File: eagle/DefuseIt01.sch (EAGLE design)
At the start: 32 parts, among them IC1 74HCT138N, IC2 74HCT138N, IC3 74HCT245N, J1 22-27-2061-06, J10 22-27-2061-06, J11 22-27-2061-06, J12 22-27-2061-06, J13 22-27-2061-06, J14 22-27-2061-06, J15 22-27-2061-06, J16 22-27-2061-06, J17 22-27-2021-02, J18 22-27-2031-03, J19 22-27-2031-03, J2 22-27-2061-06, J20 22-27-2021-02, J3 22-27-2061-06, J4 22-27-2061-06, J5 22-27-2061-06, J6 22-27-2061-06, J7 22-27-2061-06, J8 22-27-2061-06, J9 22-27-2061-06

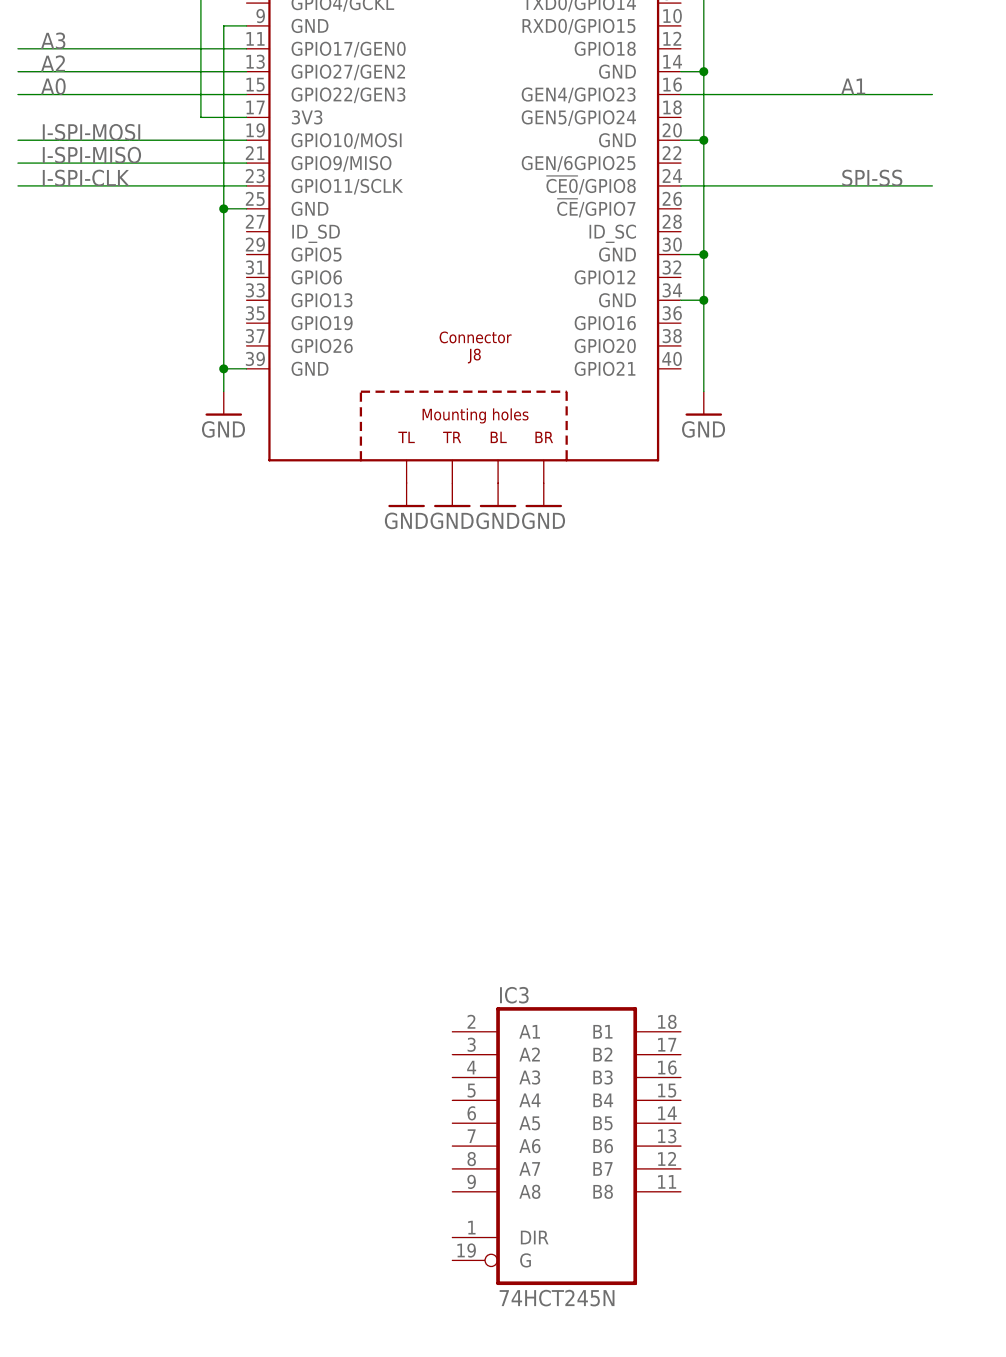
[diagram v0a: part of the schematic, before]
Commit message: Finished first layout w/o audio
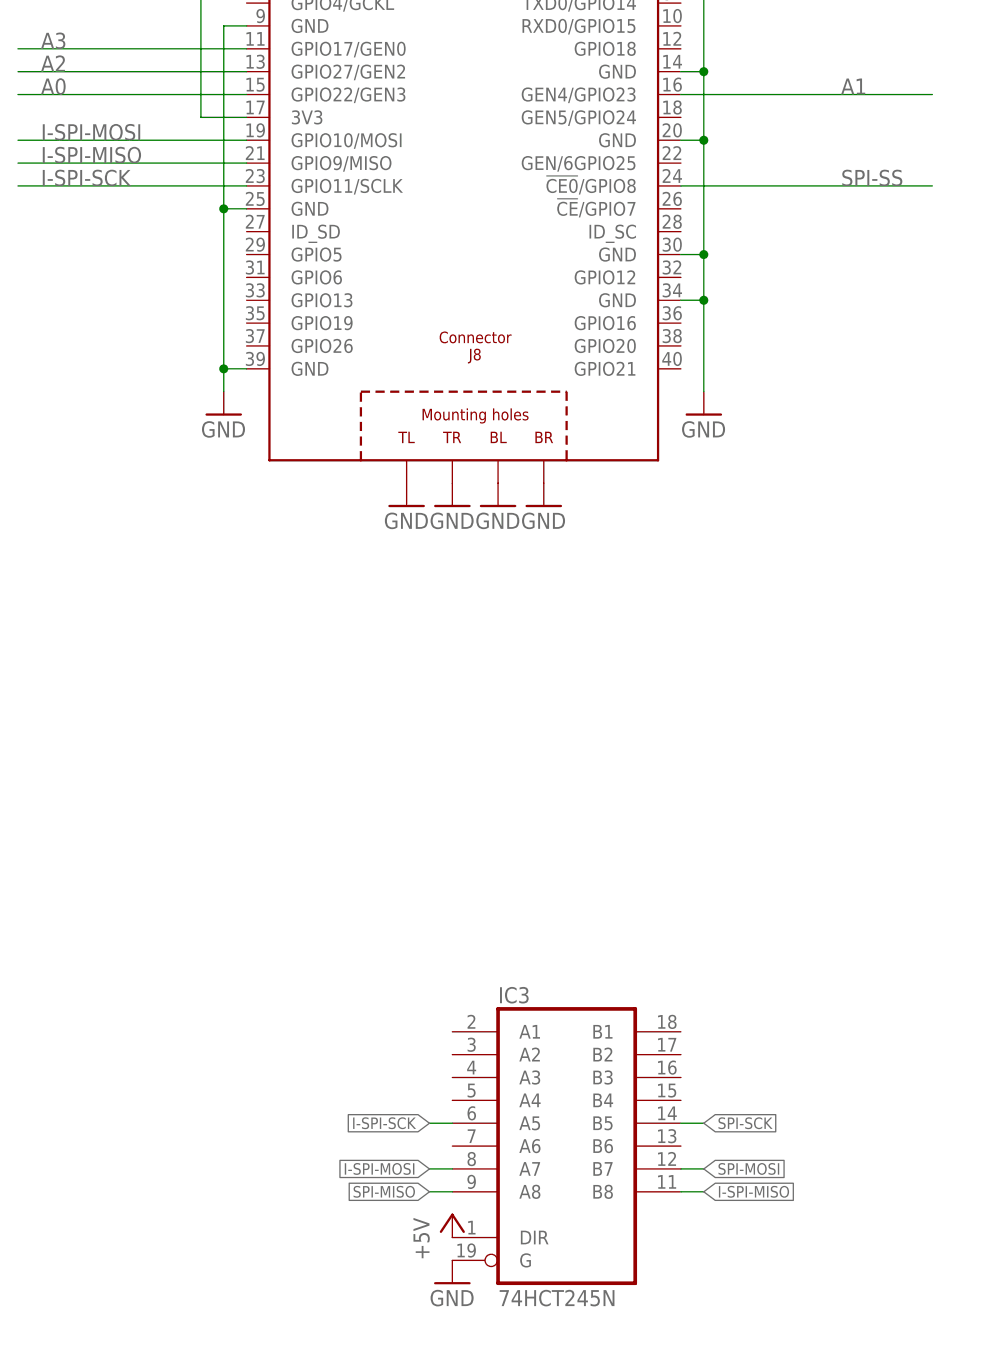
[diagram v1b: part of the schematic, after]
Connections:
- removed net I-SPI-CLK: PCB1.GPIO11/SCLK
- new net I-SPI-SCK: IC3A.A5, PCB1.GPIO11/SCLK
- new net SPI-SCK: IC3A.B5
- net +5V: now also IC3A.DIR
- net GND: now also IC3A.G
- net I-SPI-MISO: now also IC3A.B8
- net I-SPI-MOSI: now also IC3A.A7
- net SPI-MISO: now also IC3A.A8
- net SPI-MOSI: now also IC3A.B7
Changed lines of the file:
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@@
 <part name="J17" library="con-molex" deviceset="22-?-02" device="27-2021"/>
 <part name="J20" library="con-molex" deviceset="22-?-02" device="27-2021"/>
+<part name="P+7" library="supply1" deviceset="+5V" device=""/>
+<part name="GND11" library="supply1" deviceset="GND" device=""/>
 </parts>
 <sheets>
@@
 <instance part="J15" gate="-6" x="200.66" y="17.78" rot="R270"/>
 <instance part="J16" gate="-6" x="200.66" y="7.62" rot="R270"/>
+<instance part="P+7" gate="1" x="55.88" y="-7.62"/>
+<instance part="GND11" gate="1" x="55.88" y="-15.24"/>
 </instances>
 <busses>
@@
 <junction x="226.06" y="149.86"/>
 </segment>
+<segment>
+<pinref part="IC3" gate="A" pin="G"/>
+<pinref part="GND11" gate="1" pin="GND"/>
+</segment>
 </net>
 <net name="+5V" class="0">
@@
 <wire x1="220.98" y1="172.72" x2="220.98" y2="160.02" width="0.1524" layer="91"/>
 <junction x="220.98" y="160.02"/>
+</segment>
+<segment>
+<pinref part="IC3" gate="A" pin="DIR"/>
+<pinref part="P+7" gate="1" pin="+5V"/>
 </segment>
 </net>
@@
 <label x="172.72" y="167.64" size="1.778" layer="95"/>
 </segment>
+<segment>
+<pinref part="IC3" gate="A" pin="B7"/>
+<wire x1="81.28" y1="-2.54" x2="83.82" y2="-2.54" width="0.1524" layer="91"/>
+<label x="83.82" y="-2.54" size="1.27" layer="95" xref="yes"/>
+</segment>
 </net>
 <net name="SPI-MISO" class="0">
@@
 <label x="172.72" y="165.1" size="1.778" layer="95"/>
 </segment>
+<segment>
+<pinref part="IC3" gate="A" pin="A8"/>
+<wire x1="55.88" y1="-5.08" x2="53.34" y2="-5.08" width="0.1524" layer="91"/>
+<label x="53.34" y="-5.08" size="1.27" layer="95" rot="R180" xref="yes"/>
+</segment>
 </net>
 <net name="I-SPI-MOSI" class="0">
@@
 <label x="10.16" y="111.76" size="1.778" layer="95"/>
 </segment>
+<segment>
+<pinref part="IC3" gate="A" pin="A7"/>
+<wire x1="55.88" y1="-2.54" x2="53.34" y2="-2.54" width="0.1524" layer="91"/>
+<label x="53.34" y="-2.54" size="1.27" layer="95" rot="R180" xref="yes"/>
+</segment>
 </net>
 <net name="I-SPI-MISO" class="0">
@@
 <label x="10.16" y="109.22" size="1.778" layer="95"/>
 </segment>
-</net>
-<net name="I-SPI-CLK" class="0">
+<segment>
+<pinref part="IC3" gate="A" pin="B8"/>
+<wire x1="81.28" y1="-5.08" x2="83.82" y2="-5.08" width="0.1524" layer="91"/>
+<label x="83.82" y="-5.08" size="1.27" layer="95" xref="yes"/>
+</segment>
+</net>
+<net name="I-SPI-SCK" class="0">
 <segment>
 <pinref part="PCB1" gate="G$1" pin="GPIO11/SCLK"/>
@@
 <label x="10.16" y="106.68" size="1.778" layer="95"/>
 </segment>
-</net>
+<segment>
+<pinref part="IC3" gate="A" pin="A5"/>
+<wire x1="55.88" y1="2.54" x2="53.34" y2="2.54" width="0.1524" layer="91"/>
+<label x="53.34" y="2.54" size="1.27" layer="95" rot="R180" xref="yes"/>
+</segment>
+</net>
+<net name="SPI-SCK" class="0">
+<segment>
+<pinref part="IC3" gate="A" pin="B5"/>
+<wire x1="81.28" y1="2.54" x2="83.82" y2="2.54" width="0.1524" layer="91"/>
+<label x="83.82" y="2.54" size="1.27" layer="95" xref="yes"/>
+</segment>
+</net>

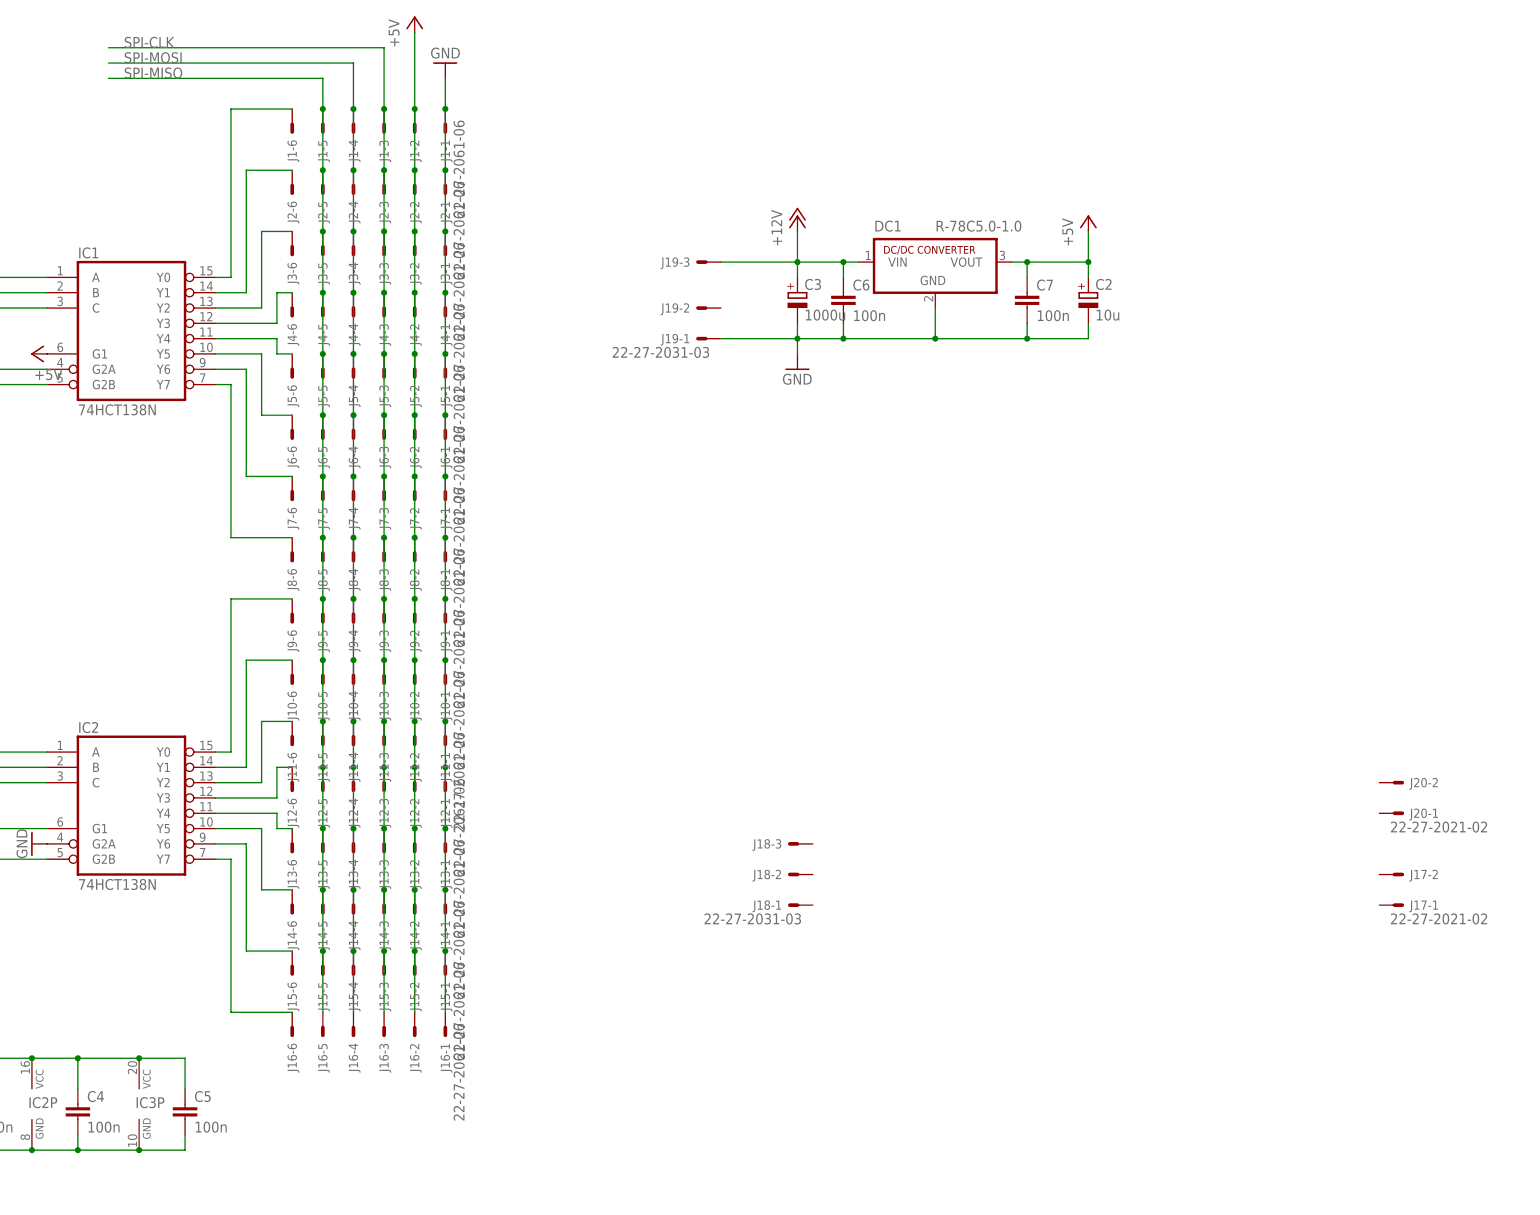
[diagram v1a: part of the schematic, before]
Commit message: added audio chip; layout correction
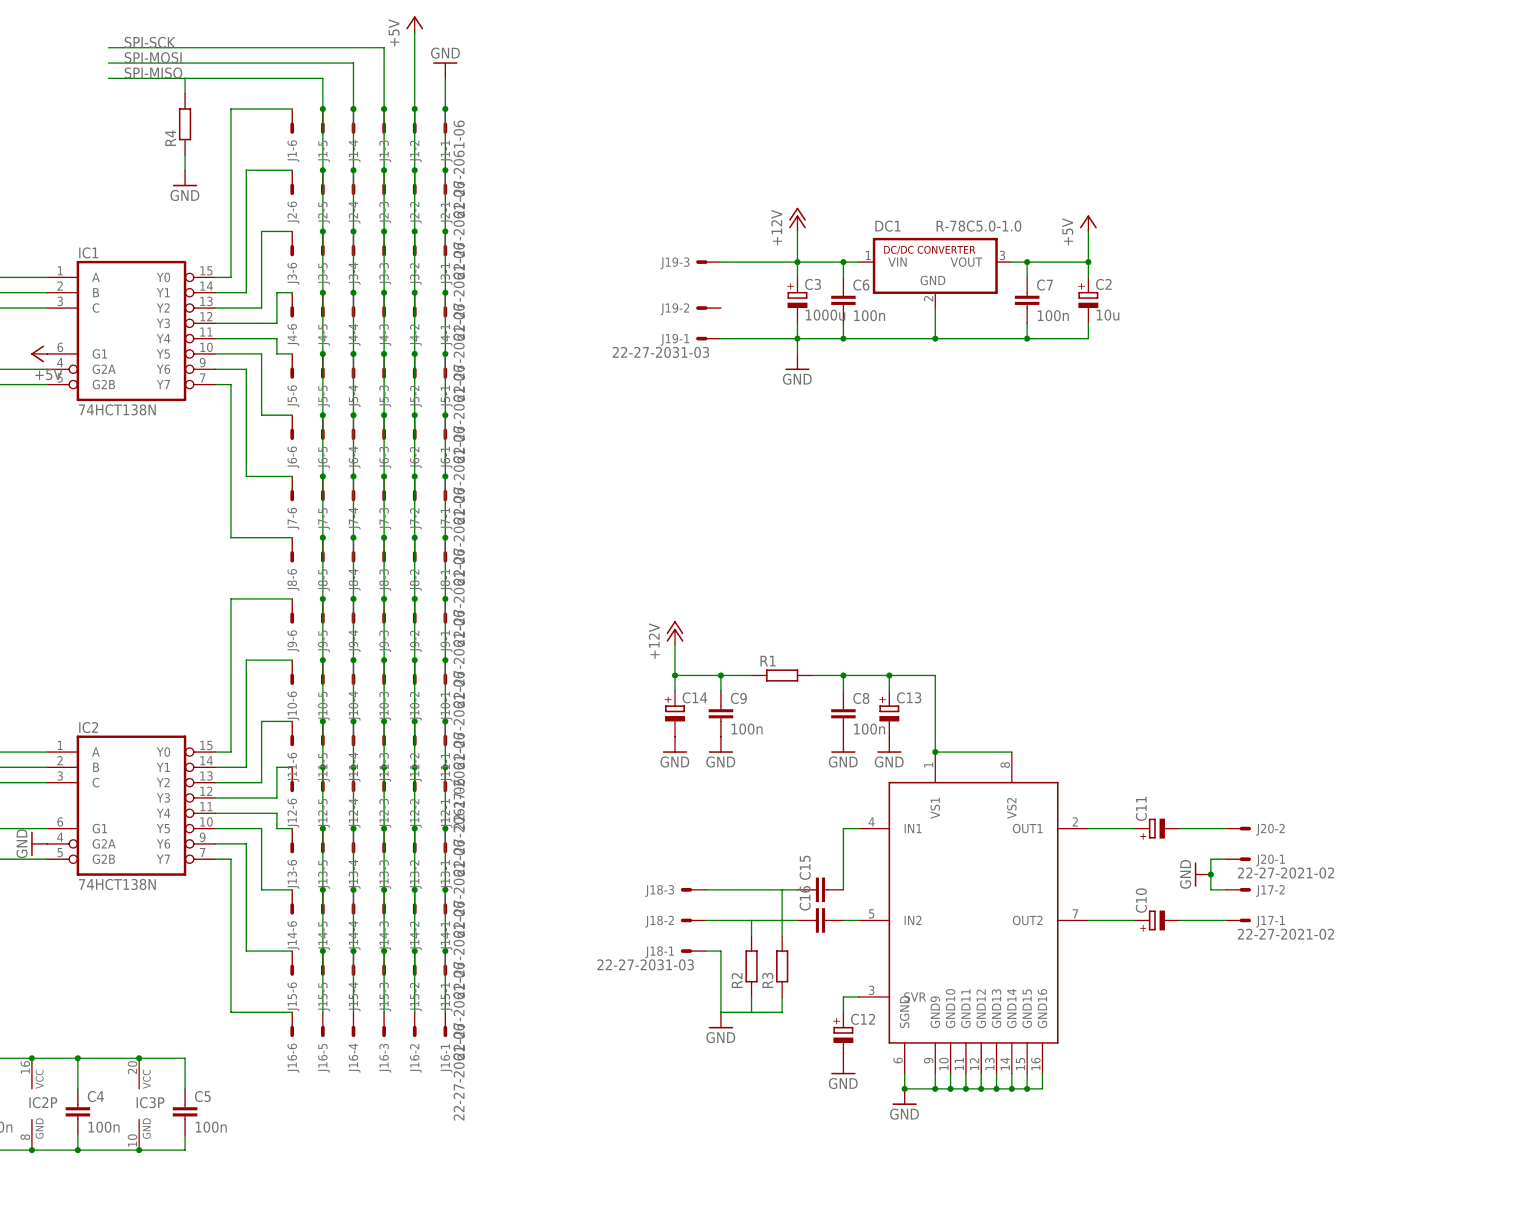
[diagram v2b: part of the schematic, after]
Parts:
- added C10, C11: (no value), rcl:CPOL-EUE3.5-8
- added C12, C13, C14: (no value), rcl:CPOL-EUE2.5-5
- added C15, C16: (no value), rcl:C-EU050-030X075
- added C8, C9: 100n, rcl:C-EU025-025X050
- added R1, R2, R3, R4: (no value), rcl:R-EU_0207/10
- added U$1: TDA7268, JKD:TDA7268
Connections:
- removed net SPI-CLK: J1-3.S, J10-3.S, J11-3.S, J12-3.S, J13-3.S, J14-3.S, J15-3.S, J16-3.S, J2-3.S, J3-3.S, J4-3.S, J5-3.S, J6-3.S, J7-3.S, J8-3.S, J9-3.S
- new net N$17: C16.2, U$1.IN2
- new net N$18: C12.+, U$1.SVR
- new net N$19: C10.+, U$1.OUT2
- new net N$20: C11.+, U$1.OUT1
- new net N$21: C11.-, J20-2.S
- new net N$22: C10.-, J17-1.S
- new net N$23: C13.+, C8.1, R1.2, U$1.VS1, U$1.VS2
- new net N$25: C15.2, U$1.IN1
- new net N$26: C16.1, J18-2.S, R2.2
- new net N$27: C15.1, J18-3.S, R3.2
- net +12V: now also C14.+, C9.1, R1.1
- net GND: now also C12.-, C13.-, C14.-, C8.2, C9.2, J17-2.S, J18-1.S, J20-1.S, R2.1, R3.1, R4.1, U$1.GND10, U$1.GND11, U$1.GND12, U$1.GND13, U$1.GND14, U$1.GND15, U$1.GND16, U$1.GND9, U$1.SGND
- net SPI-MISO: now also R4.2
- net SPI-SCK: now also J1-3.S, J10-3.S, J11-3.S, J12-3.S, J13-3.S, J14-3.S, J15-3.S, J16-3.S, J2-3.S, J3-3.S, J4-3.S, J5-3.S, J6-3.S, J7-3.S, J8-3.S, J9-3.S
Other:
- moved on the sheet: J17-1, J17-2, J18-1, J18-2, J18-3, J20-1, J20-2
